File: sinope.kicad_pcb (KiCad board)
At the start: 2 copper layers, 46 parts, among them J1 PIOA, J2 SERIAL0, J3 PIOB, J4 SERIAL1, J5 Battery, J6 5VDC, Q1 3N3906, SW1 RESET, U1 Z80CPU, U10 MEMORY_GAL, U11 74LS157, U12 TC551001, U2 Z80CTC, U3 Z80PIO, U4 Z80SIO, U5 MAX232, U6 MAX232, U7 IO_GAL, U8 MAX695, U9 27C010, X1 3.6864Mhz

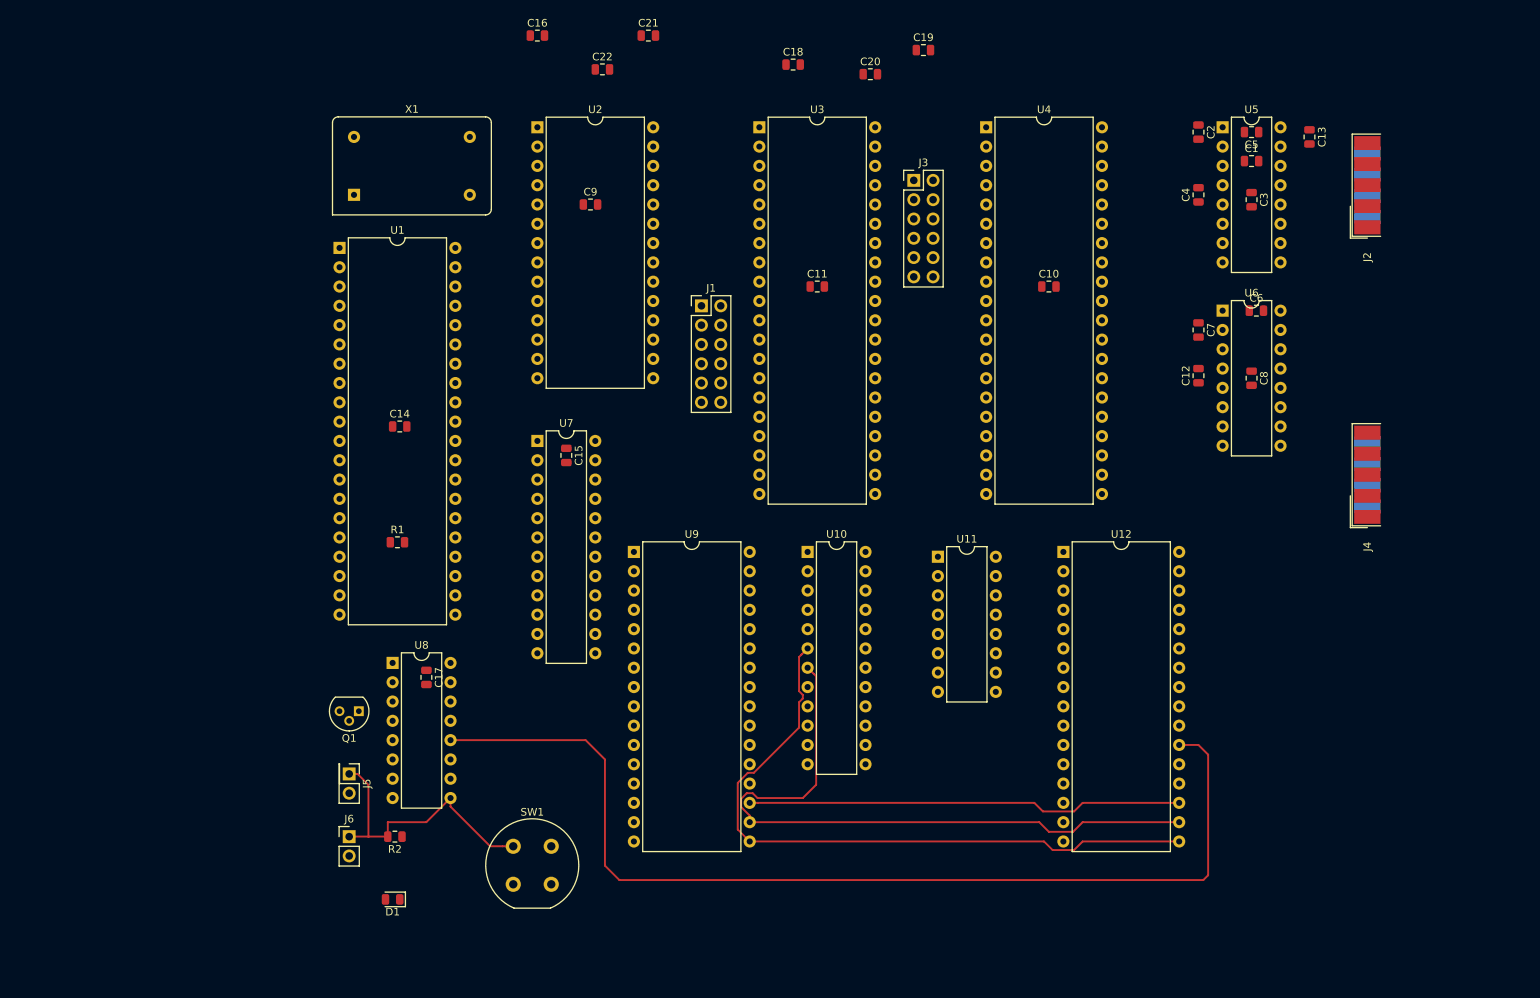
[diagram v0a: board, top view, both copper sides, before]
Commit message: PCB mostly routed
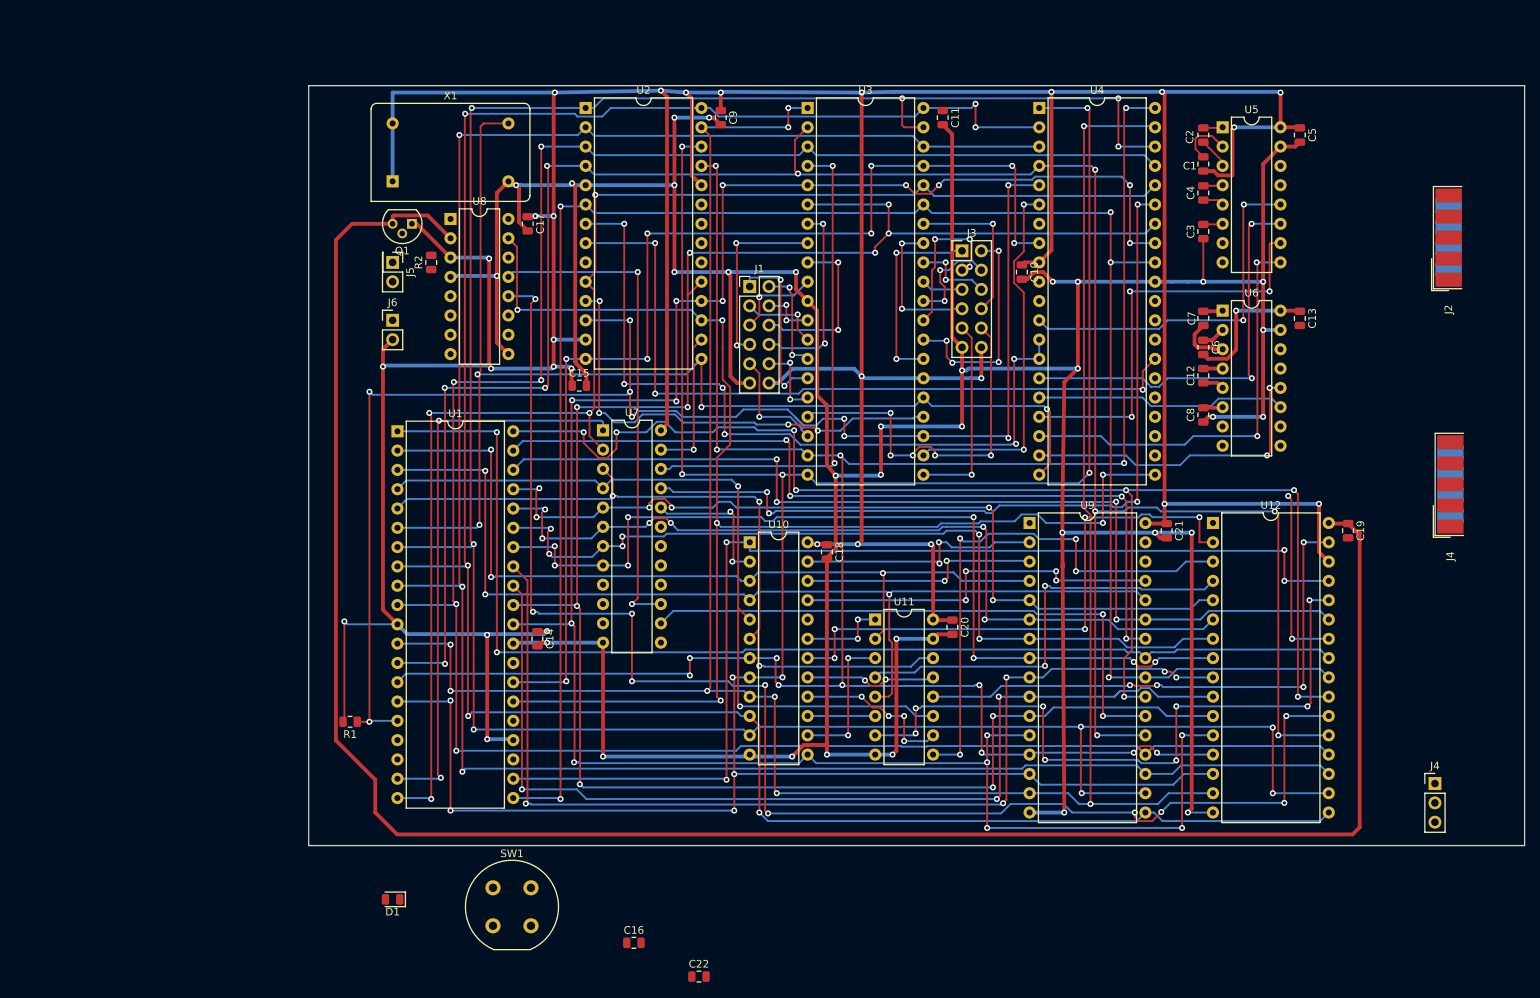
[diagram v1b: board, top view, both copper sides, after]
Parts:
- removed the J4 at (194.3, 76.2)
- added J4: SERIAL1, Connector_PinHeader_2.54mm:PinHeader_1x03_P2.54mm_Vertical, F.Cu at (203.2, 116.8)
- added J4: SERIAL1, Connector_Dsub:DSUB-9_Male_EdgeMount_P2.77mm, F.Cu at (205.2, 77.5)
- moved C22 120.1 mm to (106.3, 142.2)
- moved C16 120.1 mm to (97.8, 137.8)
- moved C21 94.3 mm to (167.9, 83.6), turned to 270 degrees
- moved C19 84.4 mm to (191.8, 83.6), turned to 270 degrees
- moved R2 75.7 mm to (71.1, 48.3), turned to 90 degrees
- moved C20 73.6 mm to (139.7, 96.3), turned to 270 degrees
- moved J6 68.2 mm to (66.0, 55.9)
- moved J5 67.6 mm to (66.0, 48.3)
- moved Q1 64.5 mm to (68.6, 43.2)
- moved C18 64.3 mm to (123.2, 86.4), turned to 270 degrees
- moved C17 61.2 mm to (83.8, 43.2)
- moved U8 58.9 mm to (73.7, 42.5)
- moved U9 52.2 mm to (149.9, 82.5)
- moved C14 33.3 mm to (85.1, 97.8), turned to 270 degrees
- moved C11 27.7 mm to (138.4, 29.2), turned to 270 degrees
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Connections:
- C10 pad 2: RAMVCC -> GND
- C11 pad 2: RAMVCC -> GND
- C13 pad 2: RAMVCC -> GND
- C14 pad 2: RAMVCC -> GND
- C15 pad 2: RAMVCC -> GND
- C16 pad 2: RAMVCC -> GND
- C17 pad 2: RAMVCC -> GND
- C18 pad 2: RAMVCC -> GND
- C19 pad 1: Net-(C19-Pad1) -> RAMVCC
- C19 pad 2: RAMVCC -> GND
- C20 pad 2: RAMVCC -> GND
- C21 pad 2: RAMVCC -> GND
- C22 pad 2: RAMVCC -> GND
- C3 pad 1: RAMVCC -> GND
- C5 pad 2: RAMVCC -> GND
- C8 pad 1: RAMVCC -> GND
- C9 pad 2: RAMVCC -> GND
- J1 pad 11: RAMVCC -> GND
- J2 pad 5: RAMVCC -> GND
- J3 pad 11: RAMVCC -> GND
- J5 pad 1: RAMVCC -> GND
- J6 pad 1: RAMVCC -> GND
- R2 pad 2: RAMVCC -> GND
- SW1 pad 1: RAMVCC -> GND
- U1 pad 29: RAMVCC -> GND
- U10 pad 10: /A14 -> /D3
- U10 pad 11: /A15 -> /D4
- U10 pad 12: RAMVCC -> GND
- U10 pad 3: /D0 -> /A12
- U10 pad 4: /D1 -> /A13
- U10 pad 5: /D2 -> /A14
- U10 pad 6: /D3 -> /A15
- U10 pad 7: /D4 -> /D0
- U10 pad 8: /A12 -> /D1
- U10 pad 9: /A13 -> /D2
- U11 pad 15: RAMVCC -> GND
- U11 pad 8: RAMVCC -> GND
- U12 pad 16: RAMVCC -> GND
- U12 pad 32: Net-(C19-Pad1) -> RAMVCC
- U2 pad 5: RAMVCC -> GND
- U3 pad 11: RAMVCC -> GND
- U4 pad 26: Net-(U4-Pad26) -> Net-(J4-Pad2)
- U4 pad 28: Net-(U4-Pad28) -> Net-(J4-Pad1)
- U4 pad 31: RAMVCC -> GND
- U5 pad 15: RAMVCC -> GND
- U6 pad 10: Net-(U4-Pad26) -> Net-(U6-Pad10)
- U6 pad 15: RAMVCC -> GND
- U6 pad 7: /TxDB -> Net-(U6-Pad7)
- U6 pad 8: /RxDB -> Net-(U6-Pad8)
- U6 pad 9: Net-(U4-Pad28) -> Net-(U6-Pad9)
- U7 pad 12: RAMVCC -> GND
- U8 pad 4: RAMVCC -> GND
- U8 pad 9: RAMVCC -> GND
- U9 pad 16: RAMVCC -> GND
- X1 pad 7: RAMVCC -> GND
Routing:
- net +5V: track 0.00 -> 665.3 mm, vias 0 -> 29
- net GND: track 0.00 -> 605.7 mm, vias 0 -> 33
- net /D1: track 0.00 -> 328.9 mm, vias 0 -> 11
- net /D2: track 0.00 -> 318.0 mm, vias 0 -> 9
- net /D7: track 0.00 -> 306.9 mm, vias 0 -> 10
- net /D0: track 0.00 -> 298.7 mm, vias 0 -> 14
- net /D6: track 0.00 -> 298.1 mm, vias 0 -> 5
- net /A0: track 0.00 -> 285.4 mm, vias 0 -> 16
- net /A1: track 0.00 -> 267.3 mm, vias 0 -> 10
- net ~RD: track 0.00 -> 255.2 mm, vias 0 -> 5
- net /D4: track 88.1 -> 334.6 mm, vias 0 -> 10
- net RAMVCC: track 38.1 -> 270.2 mm
- net /D5: track 57.4 -> 286.1 mm, vias 0 -> 3
- net /D3: track 88.2 -> 296.6 mm, vias 0 -> 6
- net ~INT: track 0.00 -> 195.1 mm, vias 0 -> 9
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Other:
- board outline added: 160 x 100 mm

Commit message: PCB work
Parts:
- removed J2: SERIAL0, Connector_Dsub:DSUB-9_Male_EdgeMount_P2.77mm
- removed the J4 at (203.2, 116.8)
- removed the J4 at (205.2, 77.5)
- added J4: SERIAL1, Connector_PinHeader_2.54mm:PinHeader_1x03_P2.54mm_Vertical, F.Cu at (196.1, 68.6)
- moved R1 44.4 mm to (71.9, 65.8)
- moved C1 4.32 mm to (177.0, 35.3)
- moved C10 4.32 mm to (153.2, 49.5)
- moved C12 4.32 mm to (177.0, 63.2)
- moved C13 4.32 mm to (189.7, 55.6)
- moved C17 4.32 mm to (88.1, 43.2)
- moved C2 4.32 mm to (177.0, 31.5)
- moved C20 4.32 mm to (144.0, 96.3)
- moved C3 4.32 mm to (177.0, 44.2)
- moved C4 4.32 mm to (177.0, 39.1)
- moved C5 4.32 mm to (189.7, 31.5)
- moved C6 4.32 mm to (177.0, 59.4)
- moved C7 4.32 mm to (177.0, 55.6)
- moved C8 4.32 mm to (177.0, 68.3)
- moved J3 4.32 mm to (145.3, 46.7)
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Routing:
- net Net-(J4-Pad1): track 0.00 -> 35.9 mm, vias 0 -> 1
- net Net-(J4-Pad2): track 0.00 -> 35.5 mm, vias 0 -> 1
- net +5V: track 665.3 -> 646.7 mm, vias 29 -> 28
- net /DCDA: track 0.00 -> 17.2 mm, vias 0 -> 1
- net GND: track 605.7 -> 621.8 mm, vias 33 -> 35
- net RAMVCC: track 270.2 -> 260.5 mm
- net ~INT: track 195.1 -> 187.6 mm
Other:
- board size 160 x 100 mm -> 173.5 x 100 mm

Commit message: PCB routed
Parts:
- added J2: SERIAL0, Connector_PinHeader_2.00mm:PinHeader_2x05_P2.00mm_Vertical, F.Cu at (194.1, 38.6)
- SW1: footprint Button_Switch_THT:Push_E-Switch_KS01Q01 -> Connector_PinHeader_2.54mm:PinHeader_1x02_P2.54mm_Vertical
- moved D1 105.1 mm to (45.5, 30.0), turned to 90 degrees
- moved SW1 95.6 mm to (46.0, 40.9), turned to 180 degrees
- moved C16 92.4 mm to (69.8, 49.7), turned to 270 degrees
- moved C22 86.6 mm to (87.9, 57.7), turned to 270 degrees
- moved R2 33.3 mm to (45.5, 33.8), turned to 270 degrees
- moved J5 29.6 mm to (46.0, 65.0), turned to 90 degrees
- moved J6 24.5 mm to (46.0, 53.1), turned to 180 degrees
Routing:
- net GND: track 621.8 -> 725.9 mm, vias 35 -> 38
- net +5V: track 646.7 -> 717.0 mm, vias 28 -> 30
- net Net-(J5-Pad2): track 0.00 -> 52.7 mm, vias 0 -> 1
- net ~RESET: track 181.6 -> 232.6 mm, vias 6 -> 8
- net /DTRA: track 0.00 -> 29.5 mm, vias 0 -> 1
- net /CTSA: track 0.00 -> 23.2 mm, vias 0 -> 1
- net /A9: track 133.2 -> 153.4 mm
- net /RTSA: track 0.00 -> 14.9 mm
- net Net-(Q1-Pad2): track 0.00 -> 14.4 mm, vias 0 -> 1
- net /DCDA: track 17.2 -> 30.0 mm
- net /TxDA: track 0.00 -> 11.8 mm, vias 0 -> 1
- net /RxDA: track 0.00 -> 9.73 mm
- net RAMVCC: track 260.5 -> 262.6 mm, vias 0 -> 1
- net Net-(D1-Pad1): track 0.00 -> 1.93 mm
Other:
- board size 173.5 x 100 mm -> 160 x 100 mm
- board text added: "+3.3V"
- board text added: "+5V"
- board text added: "BATT"
- board text added: "PWR"
- board text added: "RESET"
- board text added: "SERIAL0"
- board text added: "SERIAL1"
- board text added: "SINOPE V1.0 Hans Hübner (@hanshuebner) github.com/hanshuebner/sinope"

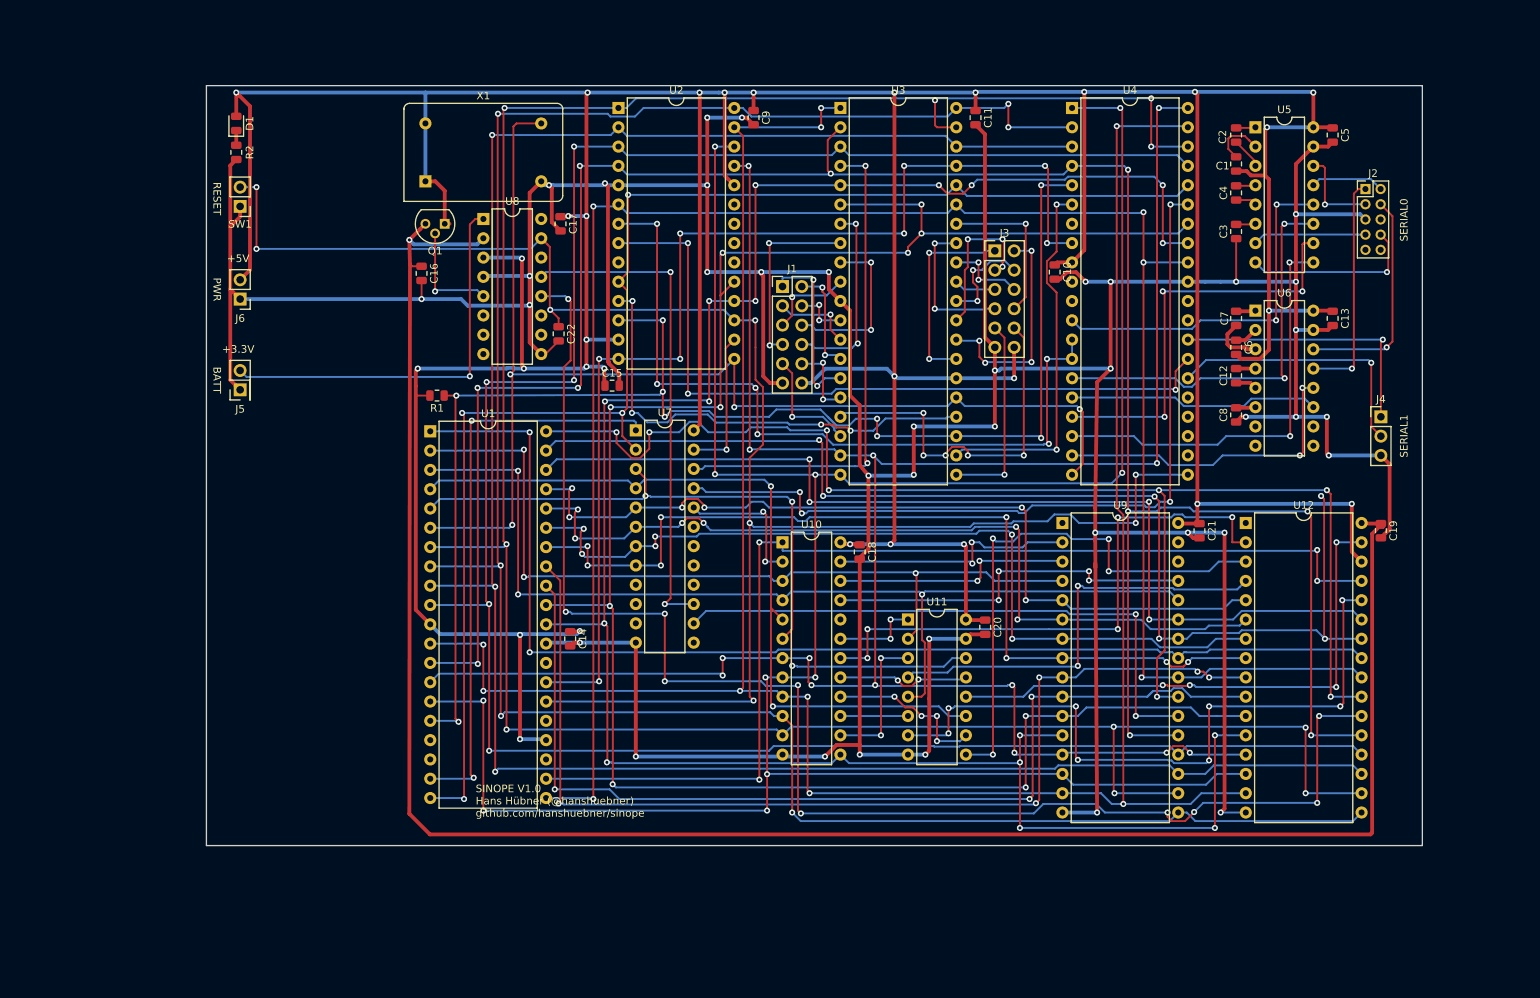
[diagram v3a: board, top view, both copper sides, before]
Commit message: Move connectors to one side.
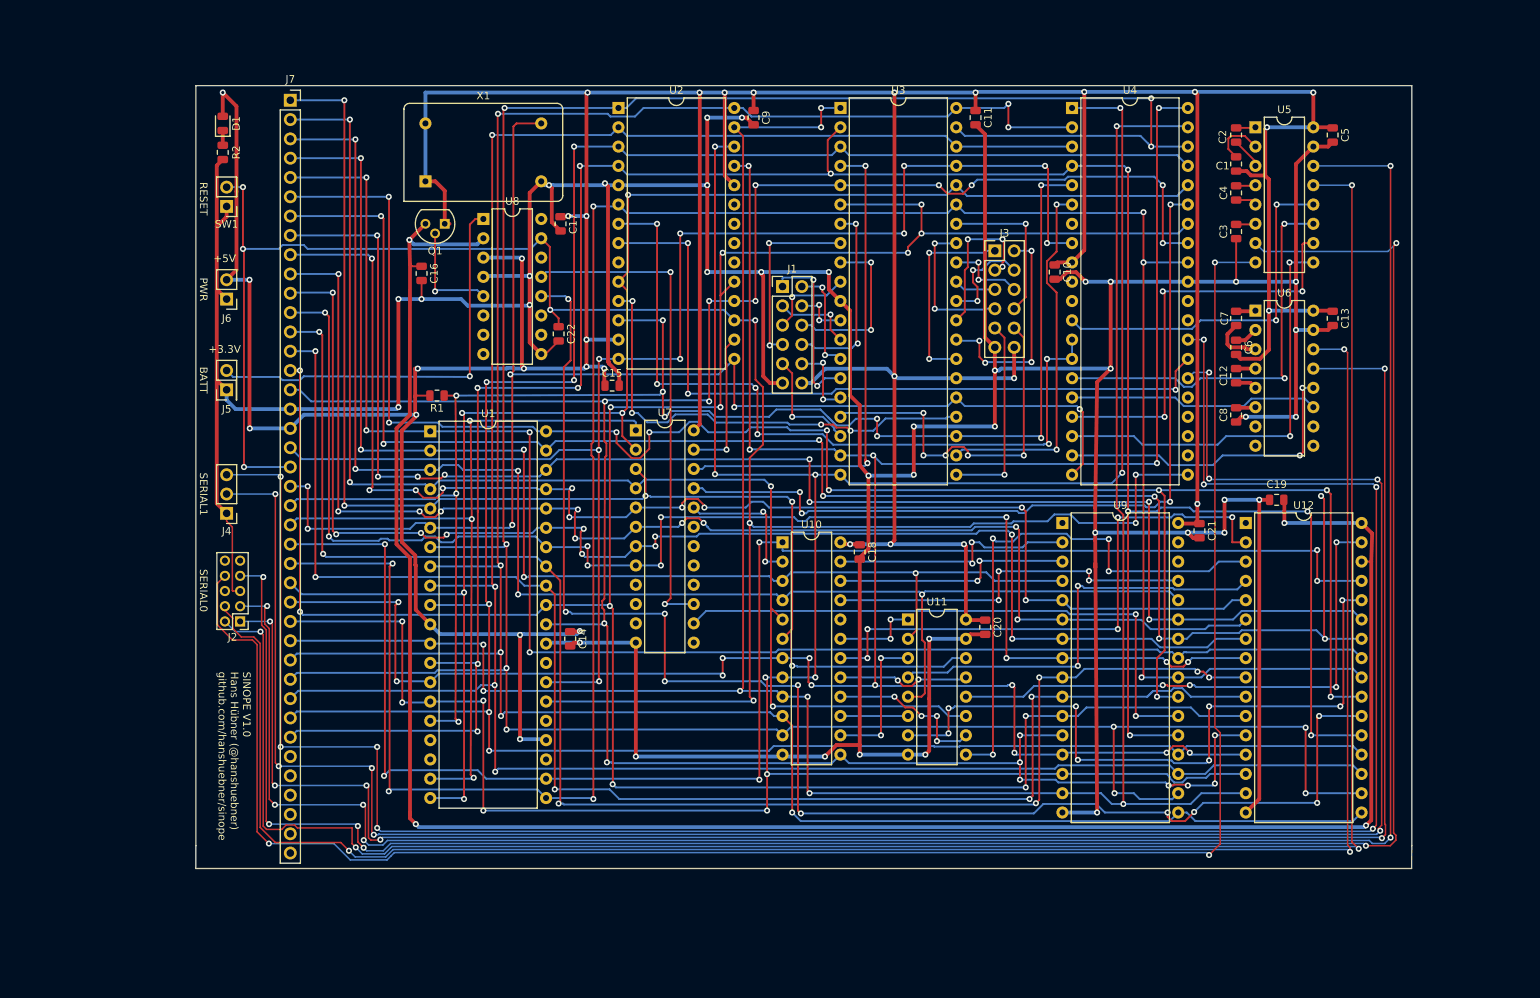
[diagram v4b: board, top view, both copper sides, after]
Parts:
- added J7: Z80_BUS, Connector_PinSocket_2.54mm:PinSocket_1x40_P2.54mm_Vertical, F.Cu at (52.6, 26.9)
- moved J2 158.6 mm to (46.0, 95.5), turned to 180 degrees
- moved J4 152.4 mm to (44.2, 81.3), turned to 180 degrees
- moved C19 14.3 mm to (182.4, 79.5), turned to 180 degrees
- moved D1 1.78 mm to (43.7, 30.0)
- moved J5 1.78 mm to (44.2, 65.0)
- moved J6 1.78 mm to (44.2, 53.1)
- moved R2 1.78 mm to (43.7, 33.8)
- moved SW1 1.78 mm to (44.2, 40.9)
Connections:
- J4 pad 1: Net-(J4-Pad1) -> GND
- J4 pad 3: GND -> Net-(J4-Pad3)
- U12 pad 30: +5V -> RAMVCC
- U4 pad 28: Net-(J4-Pad1) -> Net-(J4-Pad3)
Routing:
- net Net-(J4-Pad3): track 0.00 -> 286.9 mm, vias 0 -> 8
- net /RTSA: track 14.9 -> 286.4 mm, vias 0 -> 6
- net /TxDA: track 11.8 -> 281.6 mm, vias 1 -> 6
- net /RxDA: track 9.73 -> 271.7 mm, vias 0 -> 4
- net Net-(J4-Pad2): track 35.5 -> 283.3 mm, vias 1 -> 8
- net /CTSA: track 23.2 -> 249.3 mm, vias 1 -> 3
- net /DCDA: track 30.0 -> 250.1 mm, vias 1 -> 6
- net /DTRA: track 29.5 -> 248.0 mm, vias 1 -> 3
- net /A15: track 99.4 -> 171.3 mm, vias 3 -> 5
- net /A14: track 103.7 -> 170.2 mm, vias 2 -> 4
- net /A7: track 111.9 -> 178.1 mm, vias 6 -> 10
- net /A1: track 267.3 -> 333.4 mm, vias 10 -> 12
- net /A5: track 113.1 -> 179.2 mm, vias 6 -> 10
- net /A8: track 129.9 -> 196.0 mm, vias 4 -> 8
- net /A6: track 111.8 -> 177.5 mm, vias 6 -> 10
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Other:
- board size 160 x 100 mm -> 160 x 103 mm
